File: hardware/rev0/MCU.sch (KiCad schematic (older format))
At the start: 14 parts, among them P2 CONN_01X06, U4 STM32F048GUx

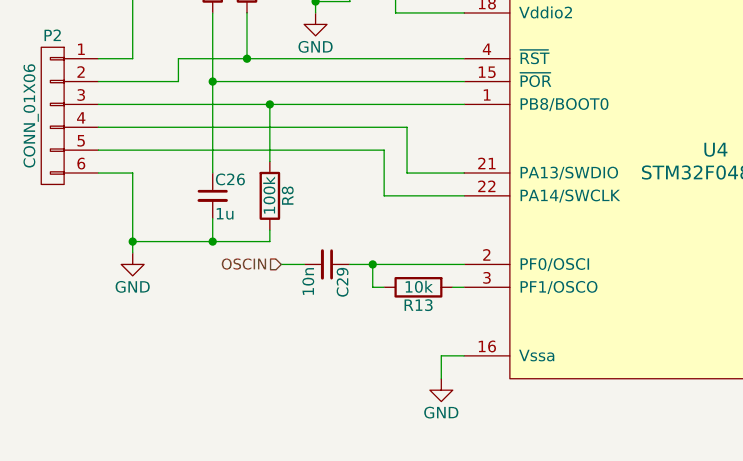
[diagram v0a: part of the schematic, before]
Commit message: Replace TCXO with XTAL
Planned TCXO became obsolete and hard to source, high quality XTAL
should be good enough with possible temperature compensation in
software.
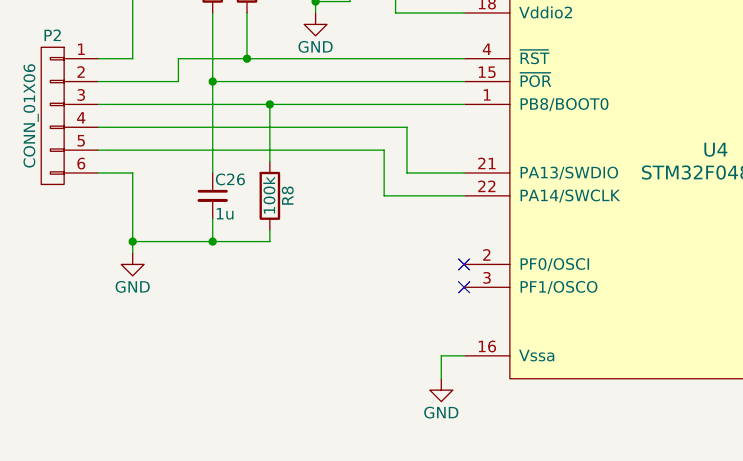
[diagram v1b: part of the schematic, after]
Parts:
- removed C29: 10n, Capacitors_SMD:C_0402, symbol C_Small
- removed R13: 10k, Resistors_SMD:R_0402, symbol R
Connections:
- no-connect marks 0 -> 2
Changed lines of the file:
@@
 	1    0    0    -1
 $EndComp
-Text HLabel 3900 3750 0    47   Input ~ 0
-OSCIN
 $Comp
 L STM32F048GUx U4
@@
 	1    5800 3300
 	1    0    0    -1
-$EndComp
-$Comp
-L C_Small C29
-U 1 1 563FC400
-P 4100 3750
-F 0 "C29" H 4110 3820 50  0000 L CNN
-F 1 "10n" H 4110 3670 50  0000 L CNN
-F 2 "Capacitors_SMD:C_0402" H 4100 3750 60  0001 C CNN
-F 3 "" H 4100 3750 60  0000 C CNN
-	1    4100 3750
-	0    1    1    0
-$EndComp
-$Comp
-L R R13
-U 1 1 563FC481
-P 4500 3850
-F 0 "R13" V 4580 3850 50  0000 C CNN
-F 1 "10k" V 4500 3850 50  0000 C CNN
-F 2 "Resistors_SMD:R_0402" V 4430 3850 30  0001 C CNN
-F 3 "" H 4500 3850 30  0000 C CNN
-	1    4500 3850
-	0    -1   1    0
 $EndComp
 $Comp
@@
 Wire Wire Line
 	4450 3150 3100 3150
-Wire Wire Line
-	4650 3850 4700 3850
-Wire Wire Line
-	4350 3850 4300 3850
-Wire Wire Line
-	4300 3850 4300 3750
-Wire Wire Line
-	4200 3750 4700 3750
-Connection ~ 4300 3750
-Wire Wire Line
-	3900 3750 4000 3750
 Connection ~ 3850 3050
 Wire Wire Line
 	3100 3050 4700 3050
+NoConn ~ 4700 3850
+NoConn ~ 4700 3750
 $EndSCHEMATC

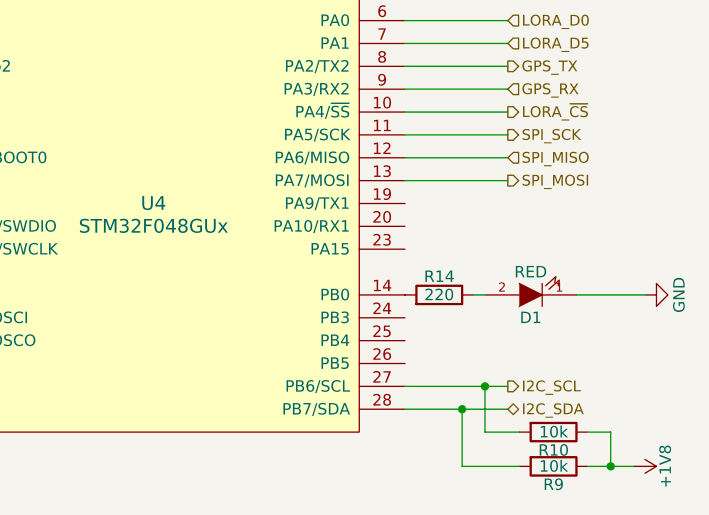
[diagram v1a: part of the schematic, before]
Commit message: DRC alterations, generate gerbers
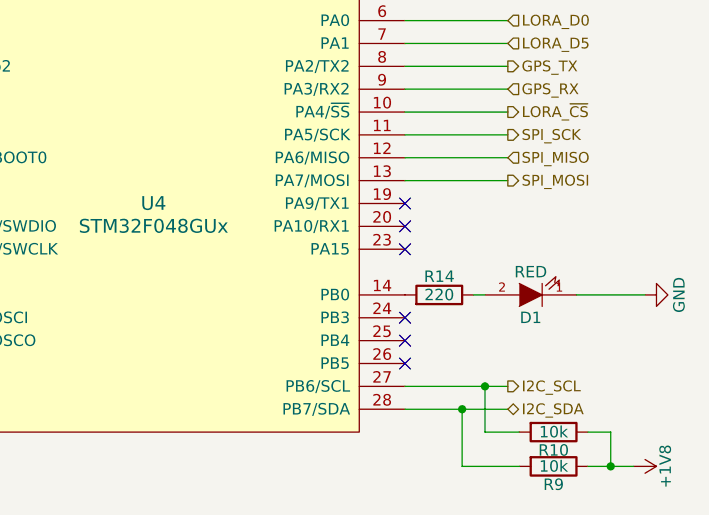
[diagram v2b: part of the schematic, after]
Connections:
- no-connect marks 2 -> 8
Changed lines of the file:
@@
 NoConn ~ 4700 3850
 NoConn ~ 4700 3750
+NoConn ~ 6900 3250
+NoConn ~ 6900 3350
+NoConn ~ 6900 3450
+NoConn ~ 6900 3750
+NoConn ~ 6900 3850
+NoConn ~ 6900 3950
 $EndSCHEMATC
